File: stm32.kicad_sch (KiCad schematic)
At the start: 59 parts, among them J1 USB_B_Mini, J4 Conn_ST_STDC14, J5 Conn_02x20_Odd_Even, J7 TC2030 - TAG Connect, Q5 SI2301CDS-T1-GE3, SW1 SW_Push, SW2 SW_Push, U3 STM32F427V_G-I_Tx, X1 8MHz 20pF

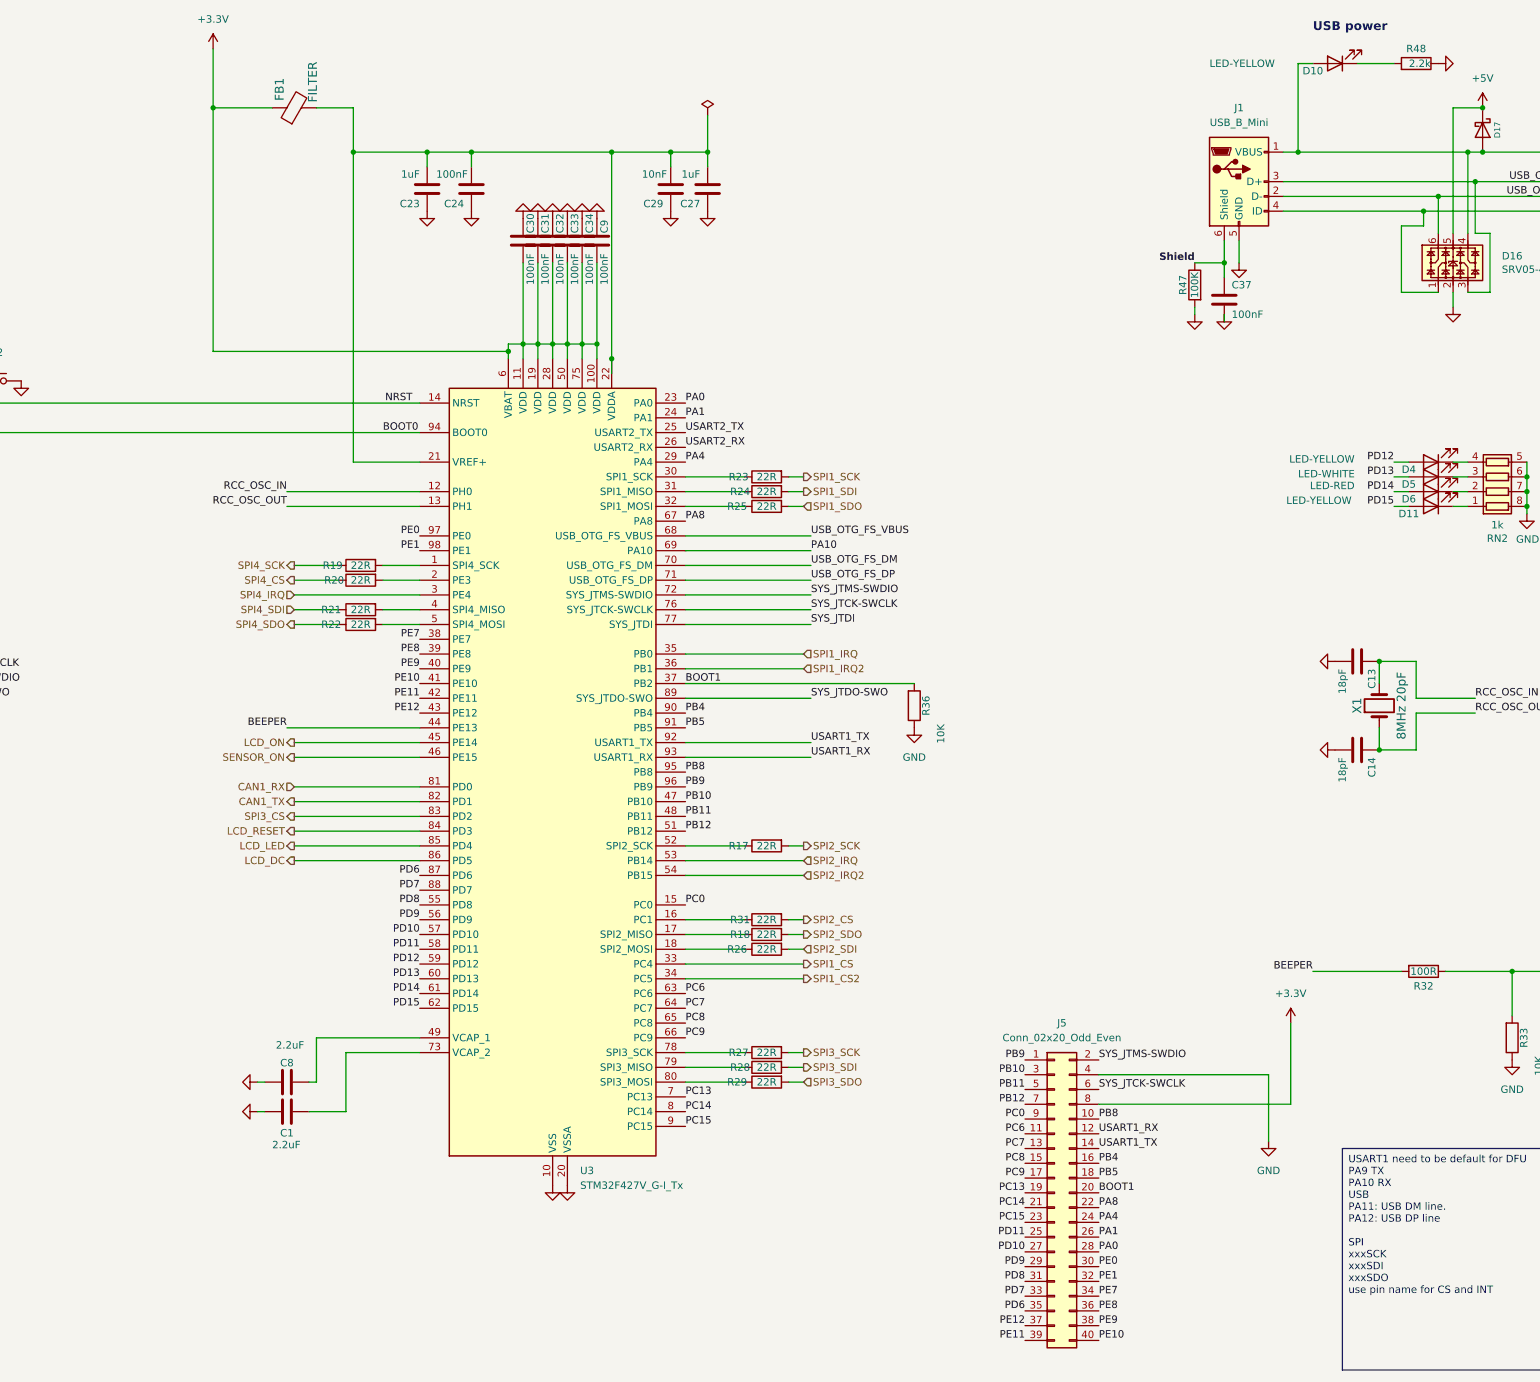
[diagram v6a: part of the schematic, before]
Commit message: changed to tp and subbed to quilter
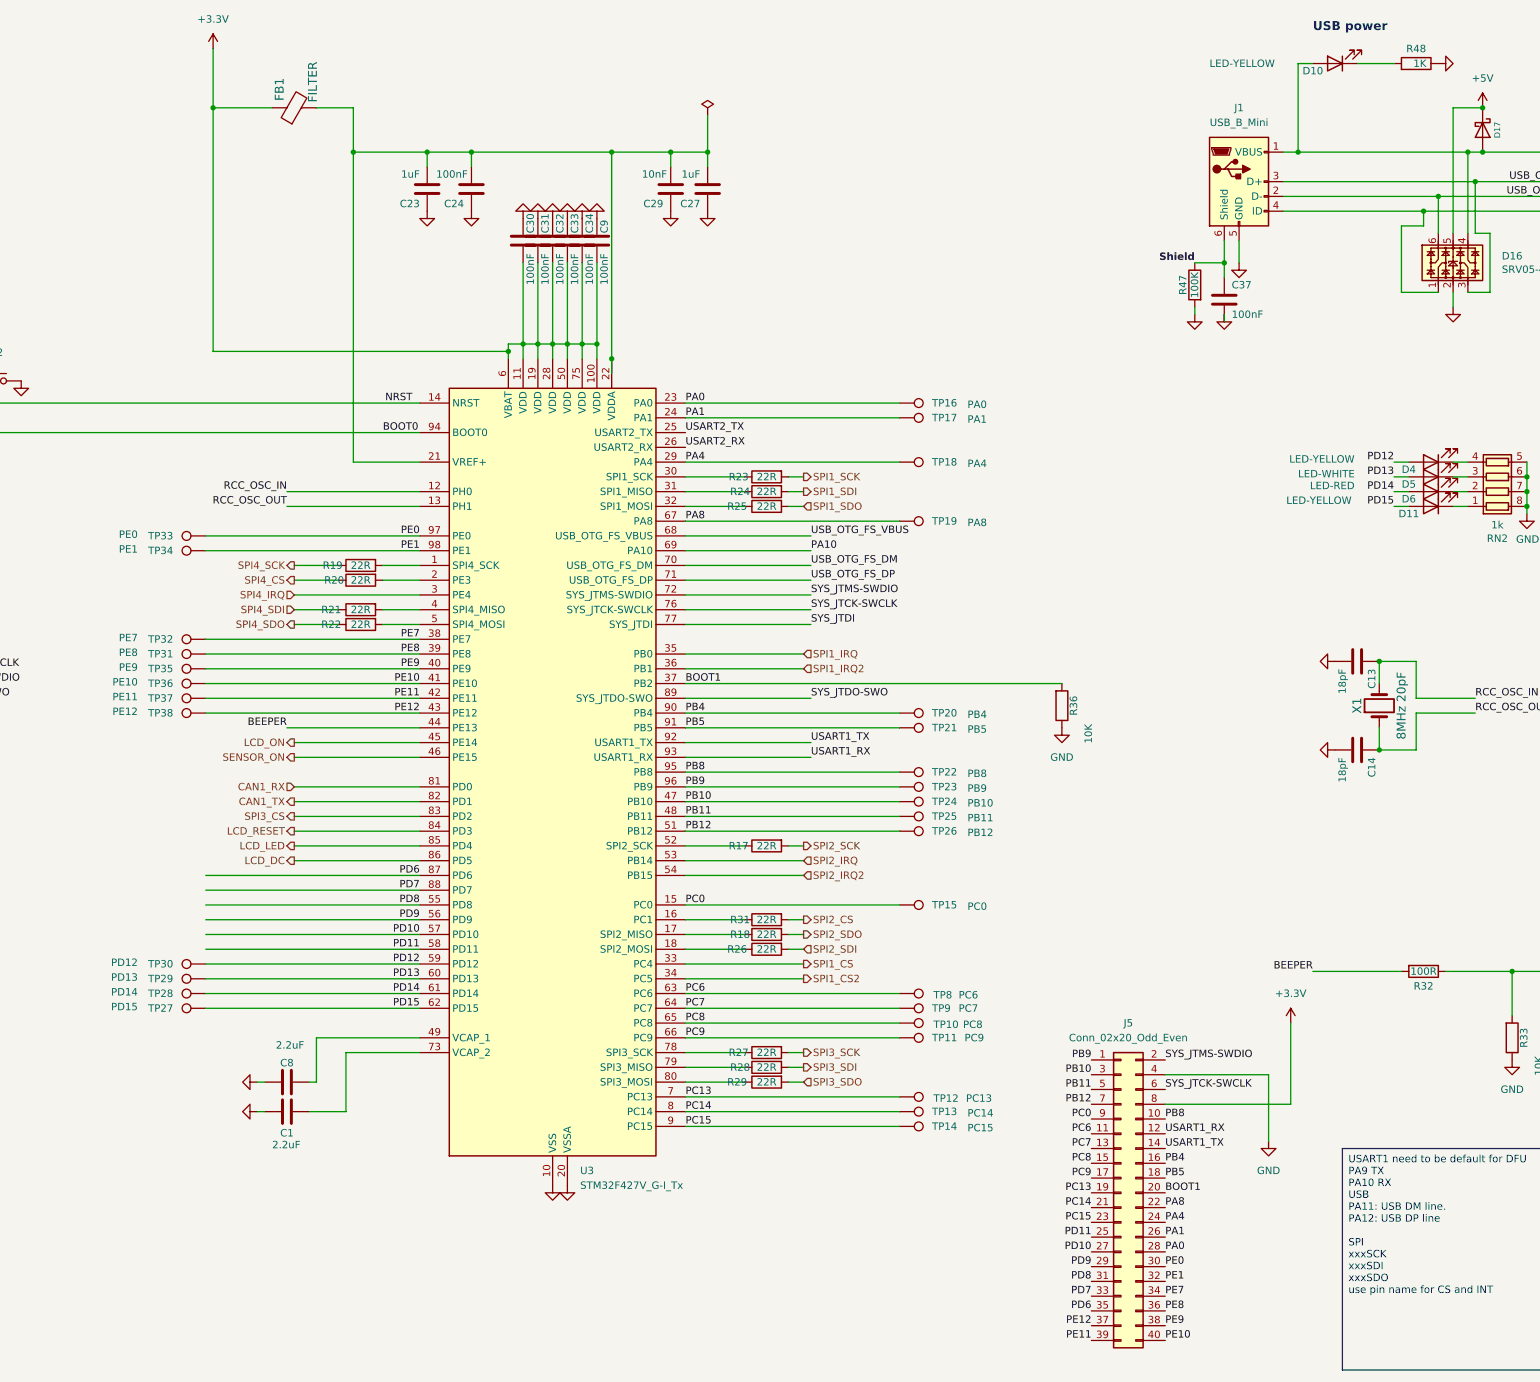
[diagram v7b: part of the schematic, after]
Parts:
- added TP10: PC8, TestPoint:TestPoint_Pad_D1.0mm, symbol Connector:TestPoint
- added TP11: PC9, TestPoint:TestPoint_Pad_D1.0mm, symbol Connector:TestPoint
- added TP12: PC13, TestPoint:TestPoint_Pad_D1.0mm, symbol Connector:TestPoint
- added TP13: PC14, TestPoint:TestPoint_Pad_D1.0mm, symbol Connector:TestPoint
- added TP14: PC15, TestPoint:TestPoint_Pad_D1.0mm, symbol Connector:TestPoint
- added TP15: PC0, TestPoint:TestPoint_Pad_D1.0mm, symbol Connector:TestPoint
- added TP16: PA0, TestPoint:TestPoint_Pad_D1.0mm, symbol Connector:TestPoint
- added TP17: PA1, TestPoint:TestPoint_Pad_D1.0mm, symbol Connector:TestPoint
- added TP18: PA4, TestPoint:TestPoint_Pad_D1.0mm, symbol Connector:TestPoint
- added TP19: PA8, TestPoint:TestPoint_Pad_D1.0mm, symbol Connector:TestPoint
- added TP20: PB4, TestPoint:TestPoint_Pad_D1.0mm, symbol Connector:TestPoint
- added TP21: PB5, TestPoint:TestPoint_Pad_D1.0mm, symbol Connector:TestPoint
- added TP22: PB8, TestPoint:TestPoint_Pad_D1.0mm, symbol Connector:TestPoint
- added TP23: PB9, TestPoint:TestPoint_Pad_D1.0mm, symbol Connector:TestPoint
- added TP24: PB10, TestPoint:TestPoint_Pad_D1.0mm, symbol Connector:TestPoint
- added TP25: PB11, TestPoint:TestPoint_Pad_D1.0mm, symbol Connector:TestPoint
- added TP26: PB12, TestPoint:TestPoint_Pad_D1.0mm, symbol Connector:TestPoint
- added TP27: PD15, TestPoint:TestPoint_Pad_D1.0mm, symbol Connector:TestPoint
- added TP28: PD14, TestPoint:TestPoint_Pad_D1.0mm, symbol Connector:TestPoint
- added TP29: PD13, TestPoint:TestPoint_Pad_D1.0mm, symbol Connector:TestPoint
- added TP30: PD12, TestPoint:TestPoint_Pad_D1.0mm, symbol Connector:TestPoint
- added TP31: PE8, TestPoint:TestPoint_Pad_D1.0mm, symbol Connector:TestPoint
- added TP32: PE7, TestPoint:TestPoint_Pad_D1.0mm, symbol Connector:TestPoint
- added TP33: PE0, TestPoint:TestPoint_Pad_D1.0mm, symbol Connector:TestPoint
- added TP34: PE1, TestPoint:TestPoint_Pad_D1.0mm, symbol Connector:TestPoint
- added TP35: PE9, TestPoint:TestPoint_Pad_D1.0mm, symbol Connector:TestPoint
- added TP36: PE10, TestPoint:TestPoint_Pad_D1.0mm, symbol Connector:TestPoint
- added TP37: PE11, TestPoint:TestPoint_Pad_D1.0mm, symbol Connector:TestPoint
- added TP38: PE12, TestPoint:TestPoint_Pad_D1.0mm, symbol Connector:TestPoint
- added TP8: PC6, TestPoint:TestPoint_Pad_D1.0mm, symbol Connector:TestPoint
- added TP9: PC7, TestPoint:TestPoint_Pad_D1.0mm, symbol Connector:TestPoint
- J5: footprint Connector_PinSocket_2.54mm:PinSocket_2x20_P2.54mm_Vertical -> Connector_PinSocket_2.00mm:PinSocket_2x20_P2.00mm_Vertical_SMD
- R48: value 2.2k -> 1K; Manufacturer StackPole -> (none); PageName stm32f407_board -> (none); Part # RMCF0603FT2K20 -> (none); VEND DIGI -> (none); VEND# RMCF0603FT2K20CT-ND -> (none)
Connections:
- net PA0: now also TP16.1
- net PA1: now also TP17.1
- net PA4: now also TP18.1
- net PA8: now also TP19.1
- net PB10: now also TP24.1
- net PB11: now also TP25.1
- net PB12: now also TP26.1
- net PB4: now also TP20.1
- net PB5: now also TP21.1
- net PB8: now also TP22.1
- net PB9: now also TP23.1
- net PC0: now also TP15.1
- net PC13: now also TP12.1
- net PC14: now also TP13.1
- net PC15: now also TP14.1
- net PC6: now also TP8.1
- net PC7: now also TP9.1
- net PC8: now also TP10.1
- net PC9: now also TP11.1
- net PD12: now also TP30.1
- net PD13: now also TP29.1
- net PD14: now also TP28.1
- net PD15: now also TP27.1
- net PE0: now also TP33.1
- net PE1: now also TP34.1
- net PE10: now also TP36.1
- net PE11: now also TP37.1
- net PE12: now also TP38.1
- net PE7: now also TP32.1
- net PE8: now also TP31.1
- net PE9: now also TP35.1
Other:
- moved on the sheet: J5, R36

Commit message: pre quilter
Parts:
- added TP39: PD10, TestPoint:TestPoint_Pad_D1.0mm, symbol Connector:TestPoint
- added TP40: PD11, TestPoint:TestPoint_Pad_D1.0mm, symbol Connector:TestPoint
- TP27: value PD15 -> PD6
- TP28: value PD14 -> PD7
- TP29: value PD13 -> PD8
- TP30: value PD12 -> PD9
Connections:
- net PD10: now also TP39.1
- net PD11: now also TP40.1
- net PD12: no longer TP30.1
- net PD13: no longer TP29.1
- net PD14: no longer TP28.1
- net PD15: no longer TP27.1
- net PD6: now also TP27.1
- net PD7: now also TP28.1
- net PD8: now also TP29.1
- net PD9: now also TP30.1
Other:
- moved on the sheet: C20, FB1, J7, R32, R43, R45, SW1, SW2
